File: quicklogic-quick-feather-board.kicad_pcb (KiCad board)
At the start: 4 copper layers, 50.8 x 22.9 mm, 21 parts, among them IC1 EOS-S3, J5 0473460001, U1 TPS62821DLCR, U2 MCP73831T-2ACI_OT, U3 MX25U6435FZNI-10G, X1 ECS-_327-12_5-34B-TR

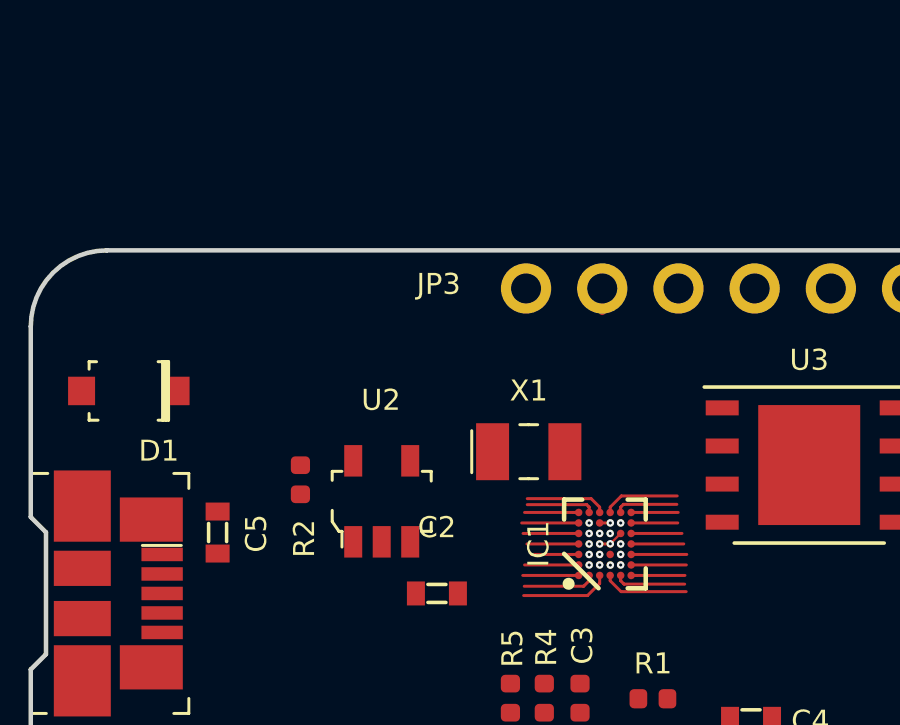
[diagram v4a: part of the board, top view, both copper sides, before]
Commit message: Package escape implemented with stacked vias
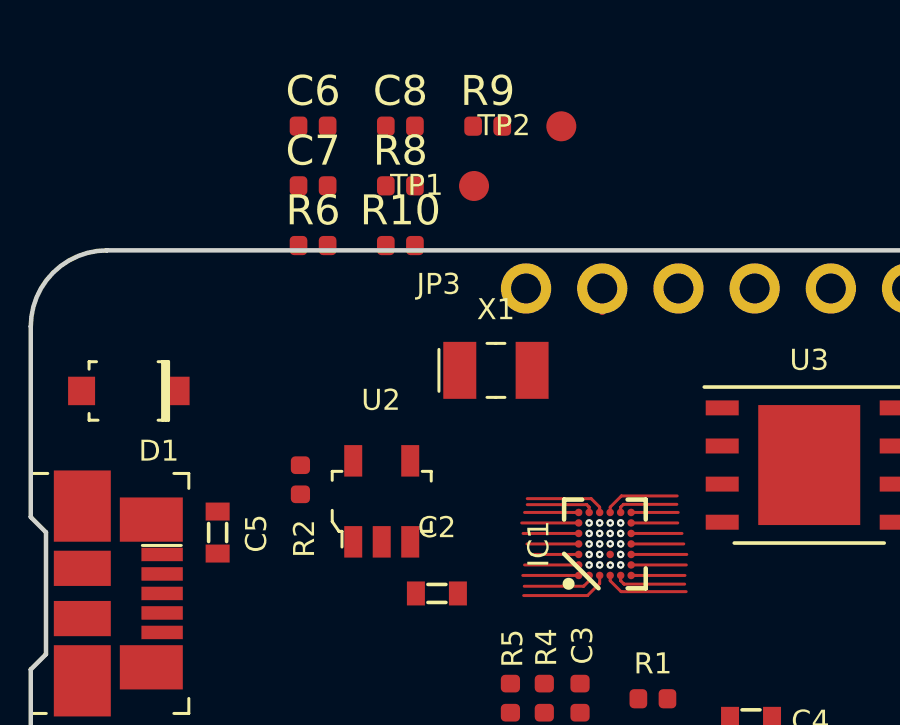
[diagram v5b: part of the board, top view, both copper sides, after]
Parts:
- added C6: C_12p_0402, antmicro-footprints:0402-cap, F.Cu at (132.5, 89.4)
- added C7: C_12p_0402, antmicro-footprints:0402-cap, F.Cu at (132.5, 91.4)
- added C8: C_100n_0402_6V3, antmicro-footprints:0402-cap, F.Cu at (135.4, 89.4)
- added R10: R_10k_0402, antmicro-footprints:0402-res, F.Cu at (135.4, 93.4)
- added R6: R_10k_0402, antmicro-footprints:0402-res, F.Cu at (132.5, 93.4)
- added R8: R_10k_0402, antmicro-footprints:0402-res, F.Cu at (135.4, 91.4)
- added R9: R_10k_0402, antmicro-footprints:0402-res, F.Cu at (138.3, 89.4)
- added TP1: TP_SMD1MM, antmicro-footprints:Testpoint_smd_1mm, F.Cu at (137.9, 91.5)
- added TP2: TP_SMD1MM, antmicro-footprints:Testpoint_smd_1mm, F.Cu at (140.8, 89.5)
- moved X1 2.92 mm to (138.6, 97.6)
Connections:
- net Net-(IC1-PadC1) renamed /SPI_SLV_MOSI
- net Net-(IC1-PadD1) renamed /SPI_SLV_MISO
- net Net-(IC1-PadD2) renamed /IO24
- net Net-(IC1-PadD3) renamed /IO25
- net Net-(IC1-PadD5) renamed /SPI_MST_CLK
- net Net-(IC1-PadD7) renamed /INT
- net Net-(IC1-PadE1) renamed /SPI_SLV_CLK
- net Net-(IC1-PadE2) renamed /IO23
- net Net-(IC1-PadE3) renamed /IO29
- net Net-(IC1-PadE4) renamed /IO31
- net Net-(IC1-PadE6) renamed /SPI_MST_MOSI
- net Net-(IC1-PadE7) renamed /SDW_IO
- net Net-(IC1-PadF2) renamed /SPI_SLV_SS
- net Net-(IC1-PadF3) renamed /IO28
- net Net-(IC1-PadF4) renamed /IO30
- net Net-(IC1-PadF5) renamed /SPI_MST_MISO
- net Net-(IC1-PadF6) renamed /SPI_MST_SS
- net Net-(IC1-PadF7) renamed /SWD_CLK
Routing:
- net /IO25: track 0.00 -> 1.50 mm, vias 0 -> 2
- net GND: track 1.38 -> 0.54 mm, vias 8 -> 13
- net /IO24: track 2.26 -> 2.92 mm
- net /SPI_MST_CLK: track 2.12 -> 1.54 mm, vias 1 -> 3
- net /EOS_VDD: track 6.03 -> 6.55 mm, vias 3 -> 4
- added copper zone on In2.Cu, net GND
- removed copper zone on In1.Cu, net GND

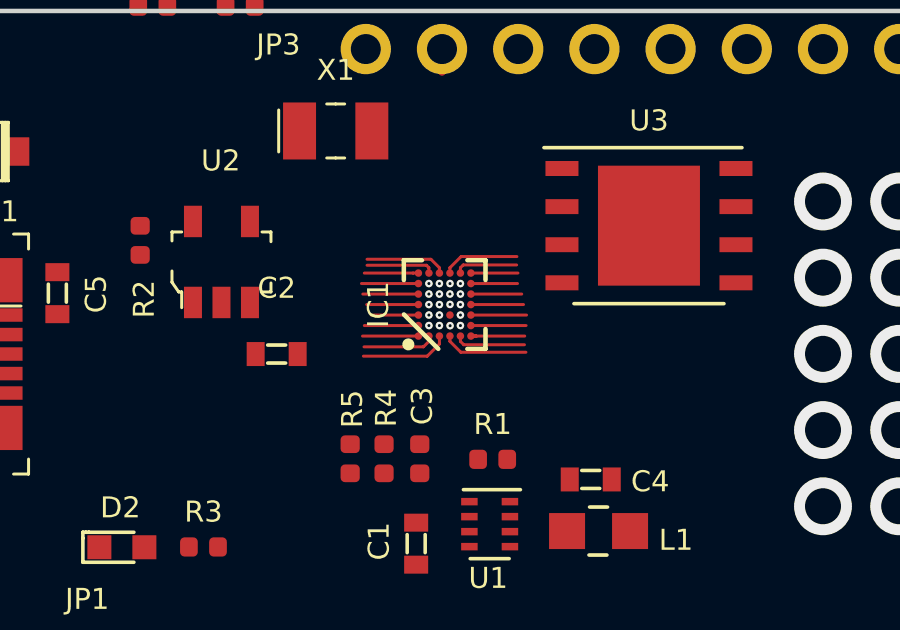
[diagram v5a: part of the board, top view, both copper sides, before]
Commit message: Board stackup changed to 6L, added GND+PWR plane
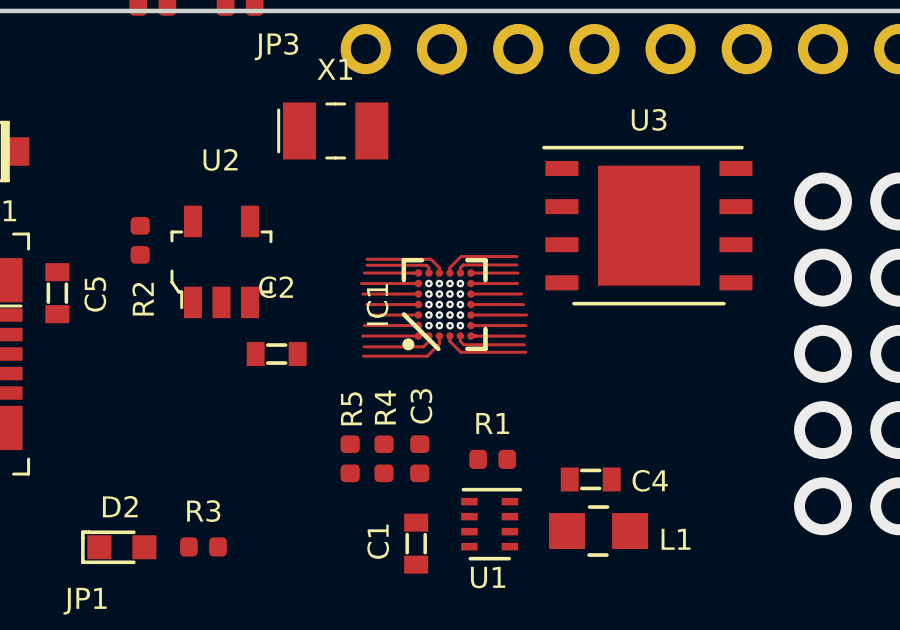
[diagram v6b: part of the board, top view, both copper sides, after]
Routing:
- net /IO25: vias 2 -> 3
- added copper zone on In3.Cu, net /3V3_SYS
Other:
- copper layers 4 -> 6
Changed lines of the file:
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@@
     (thickness 1.6)
     (drawings 30)
-    (tracks 160)
+    (tracks 161)
     (zones 0)
     (modules 30)
@@
   (layers
     (0 Top signal)
-    (1 In1.Cu signal)
-    (2 In2.Cu signal)
+    (1 In1.Cu signal hide)
+    (2 In2.Cu mixed hide)
+    (3 In3.Cu power)
+    (4 In4.Cu signal hide)
     (31 Bottom signal hide)
     (32 B.Adhes user hide)
@@
     (42 Eco1.User user hide)
     (43 Eco2.User user hide)
-    (44 Edge.Cuts user hide)
+    (44 Edge.Cuts user)
     (45 Margin user hide)
     (46 B.CrtYd user hide)
@@
       (drillshape 0)
       (scaleselection 1)
-      (outputdirectory ""))
+      (outputdirectory "Gerbers"))
   )
   (net 0 "")
@@
     (arrow2b (pts (xy 118.6561 94.8436) (xy 119.242521 95.970104)))
   )
+  (via micro (at 142.4178 103.7082) (size 0.25) (drill 0.1) (layers Top In1.Cu) (net 113))
   (via micro (at 143.3703 104.3559) (size 0.25) (drill 0.1) (layers In1.Cu In2.Cu) (net 113))
   (via micro (at 143.3957 102.362) (size 0.25) (drill 0.1) (layers In1.Cu In2.Cu) (net 108))
@@
       )
     )
+  )
+  (zone (net 1) (net_name GND) (layer In2.Cu) (hatch full 0.508)
+    (connect_pads (clearance 0.0762))
+    (min_thickness 0.254)
+    (fill yes (arc_segments 32) (thermal_gap 0.508) (thermal_bridge_width 0.508))
+    (polygon
+      (pts
+        (xy 123.1392 93.599) (xy 173.9773 93.4974) (xy 173.99 116.4209) (xy 123.063 116.4209)
+      )
+    )
+  )
+  (zone (net 90) (net_name /3V3_SYS) (layer In3.Cu) (hatch full 0.508)
+    (connect_pads (clearance 0.0762))
+    (min_thickness 0.254)
+    (fill yes (arc_segments 32) (thermal_gap 0.508) (thermal_bridge_width 0.508))
+    (polygon
+      (pts
+        (xy 123.1646 93.5482) (xy 173.9011 93.6117) (xy 173.9011 116.4463) (xy 123.0757 116.4336)
+      )
+    )

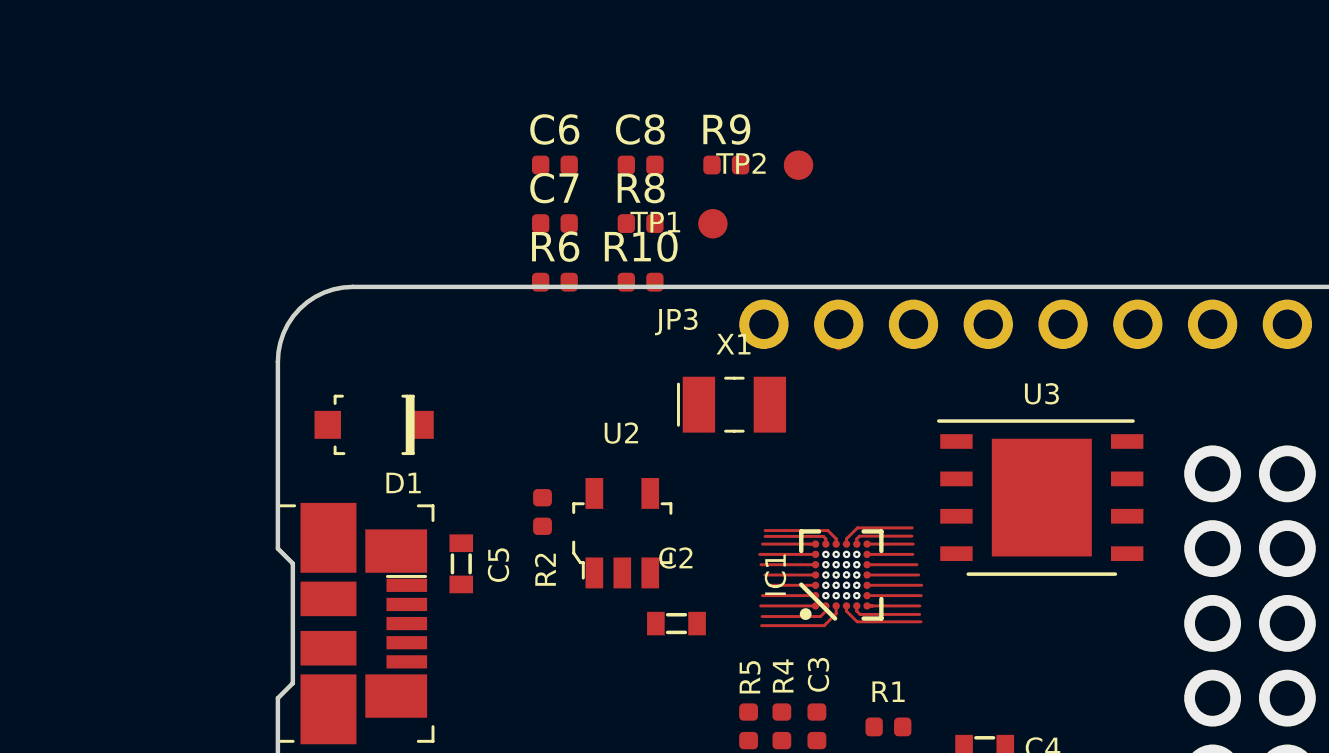
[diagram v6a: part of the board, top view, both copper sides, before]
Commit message: Changed flash memory, connected missing nets, cleanup
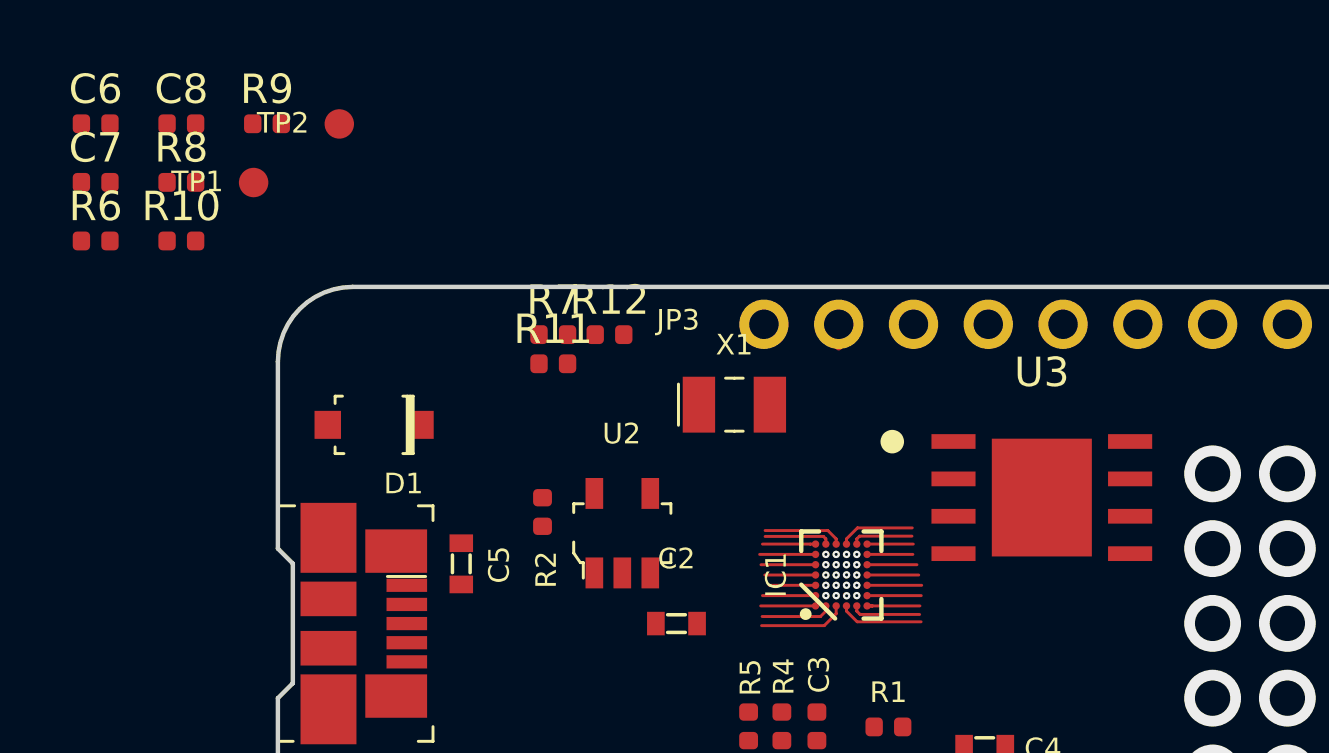
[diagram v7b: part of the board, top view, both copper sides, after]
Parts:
- added R11: R_22R_0402, antmicro-footprints:0402-res, F.Cu at (132.5, 96.2)
- added R12: R_10k_0402, antmicro-footprints:0402-res, F.Cu at (134.4, 95.2)
- added R7: R_22R_0402, antmicro-footprints:0402-res, F.Cu at (132.5, 95.2)
- R9: value R_10k_0402 -> R_1k5_0402
- U3: value MX25U6435FZNI-10G -> GD25Q16CWIGR; footprint antmicro-footprints:DFN-8-1EP_6x5mm_P1.27mm_EP4x3.4mm -> antmicro-footprints:GD25Q16CWIG
- moved TP1 15.7 mm to (122.3, 90.1)
- moved TP2 15.7 mm to (125.2, 88.1)
- moved C6 15.7 mm to (116.9, 88.0)
- moved C7 15.7 mm to (116.9, 90.0)
- moved C8 15.7 mm to (119.8, 88.0)
- moved R10 15.7 mm to (119.8, 92.0)
- moved R6 15.7 mm to (116.9, 92.0)
- moved R8 15.7 mm to (119.8, 90.0)
- moved R9 15.7 mm to (122.7, 88.0)
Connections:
- net Net-(R10-Pad2) renamed /SPI_WP
- C8 pad 1: GND -> /3V3_SYS
- C8 pad 2: /1V8_SYS -> GND
- IC1 pad B3: /EOS_VDD -> /3V3_SYS
- IC1 pad C2: /EOS_VDD -> /3V3_SYS
- IC1 pad C6: /EOS_VDD -> /3V3_SYS
- IC1 pad D6: /EOS_VDD -> /3V3_SYS
- IC1 pad E2: /IO23 -> /PU_CTRL_USBP
- IC1 pad E3: /IO29 -> Net-(IC1-PadE3)
- IC1 pad F3: /IO28 -> Net-(IC1-PadF3)
- R10 pad 1: /1V8_SYS -> /3V3_SYS
- R6 pad 1: /EOS_VDD -> /3V3_SYS
- R8 pad 1: /1V8_SYS -> /SPI_HOLD
- R8 pad 2: Net-(R8-Pad2) -> /3V3_SYS
- R9 pad 1: Net-(R8-Pad2) -> /PU_CTRL_USBP
- R9 pad 2: GND -> /USB_D_P
- U3 pad 1: /SPI_MASTER_SS -> /SPI_MST_SS
- U3 pad 2: /SPI_MASTER_MISO -> /SPI_MST_MISO
- U3 pad 5: /SPI_MASTER_MOSI -> /SPI_MST_MOSI
- U3 pad 6: /SPI_MASTER_SCK -> /SPI_MST_CLK
- U3 pad 7: Net-(R8-Pad2) -> /SPI_HOLD
- U3 pad 8: /1V8_SYS -> /3V3_SYS
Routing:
- net /EOS_VDD: track 6.55 -> 0.00 mm, vias 4 -> 0
- net /3V3_SYS: track 0.00 -> 6.55 mm, vias 0 -> 4
- net Net-(IC1-PadE3): track 0.00 -> 2.20 mm, vias 0 -> 1
- net /PU_CTRL_USBP: track 0.00 -> 2.20 mm, vias 0 -> 1
- net /IO29: track 2.20 -> 0.00 mm, vias 1 -> 0
- net /IO23: track 2.20 -> 0.00 mm, vias 1 -> 0
- net Net-(IC1-PadF3): track 0.00 -> 1.85 mm
- net /IO28: track 1.85 -> 0.00 mm

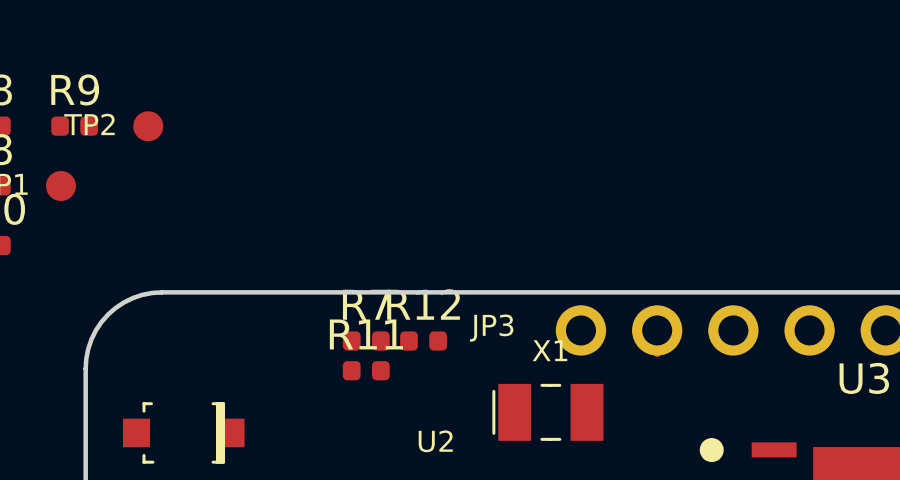
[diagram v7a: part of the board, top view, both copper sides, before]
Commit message: Added IM69D130 microphone to schematics
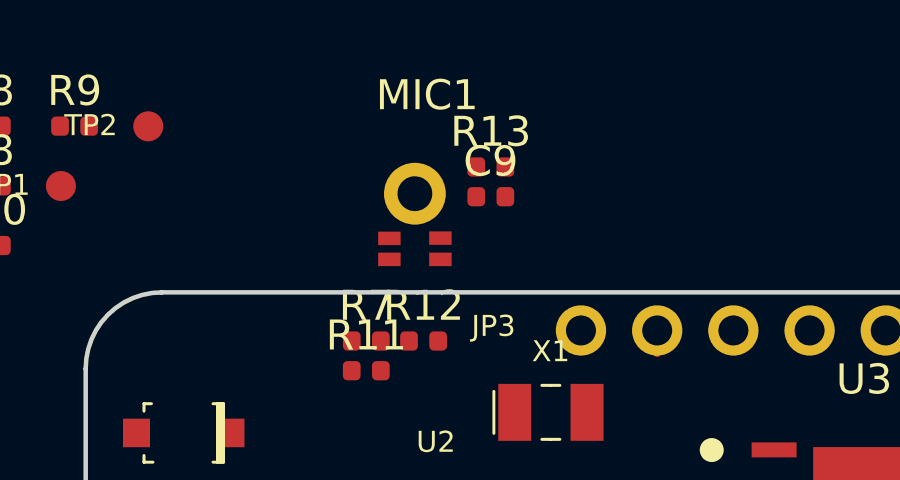
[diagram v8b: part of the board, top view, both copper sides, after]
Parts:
- added C9: C_100n_0402_6V3, antmicro-footprints:0402-cap, F.Cu at (136.6, 90.4)
- added MIC1: IM69D130, antmicro-footprints:IM69D130, F.Cu at (134.1, 90.3)
- added R13: R_100R_0402, antmicro-footprints:0402-res, F.Cu at (136.6, 89.4)
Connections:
- IC1 pad B5: Net-(IC1-PadB5) -> /MIC_DATA
- IC1 pad B6: Net-(IC1-PadB6) -> /MIC_CLOCK
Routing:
- net Net-(IC1-PadB6): track 2.38 -> 0.00 mm, vias 1 -> 0
- net /MIC_CLOCK: track 0.00 -> 2.38 mm, vias 0 -> 1
- net Net-(IC1-PadB5): track 2.25 -> 0.00 mm, vias 1 -> 0
- net /MIC_DATA: track 0.00 -> 2.25 mm, vias 0 -> 1
